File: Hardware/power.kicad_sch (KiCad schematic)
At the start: 12 parts, among them J1 Barrel_Jack_MountingPin, J2 31-M-12, Q1 AONR21321, U1 HUSB238, U2 AMS1117-3.3

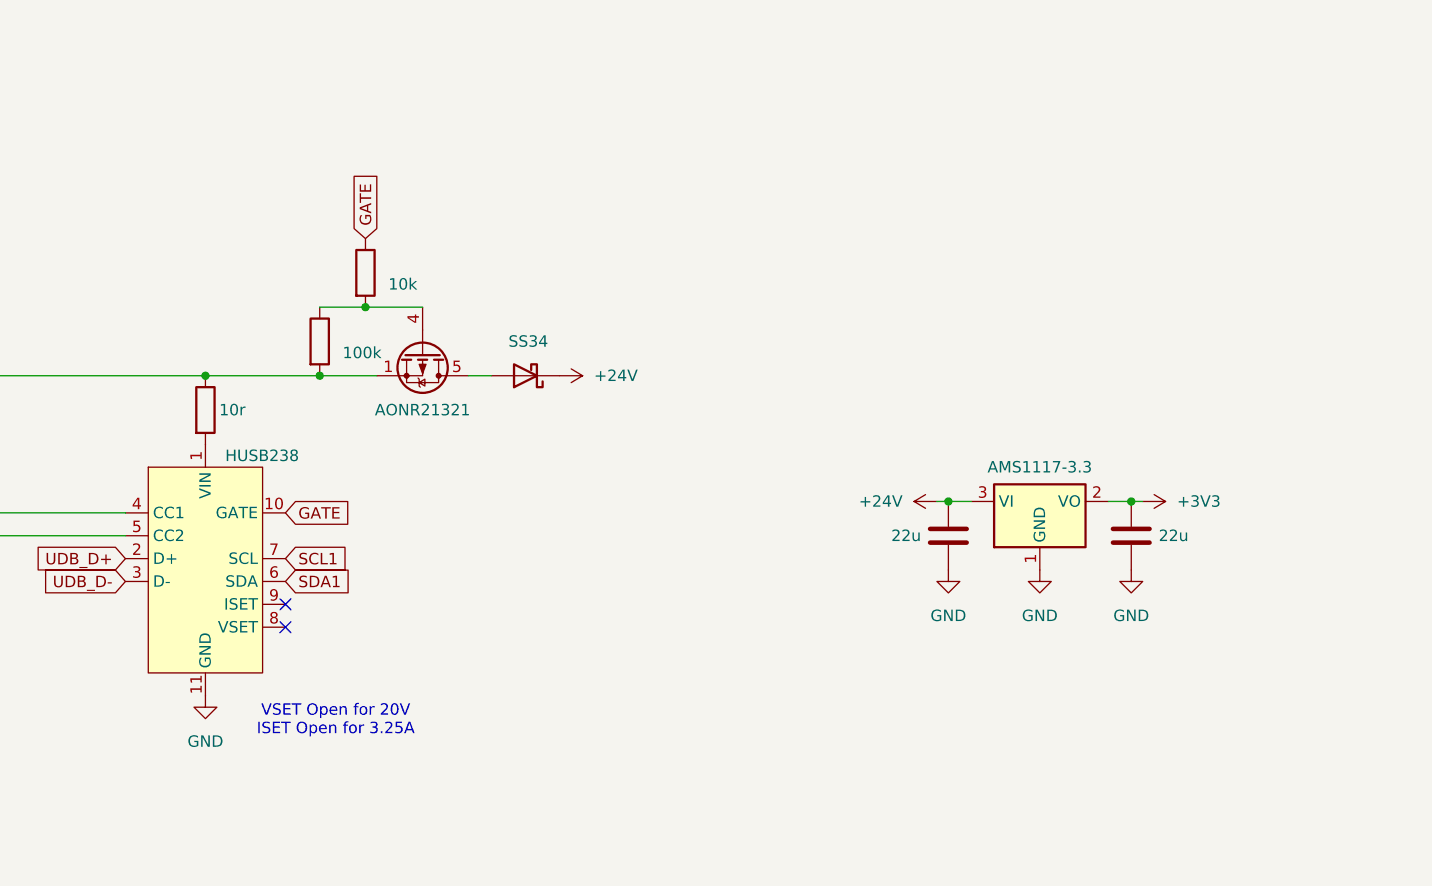
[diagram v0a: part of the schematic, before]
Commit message: Add readme, bad power routing, final heater idea. Likely needs new layout.
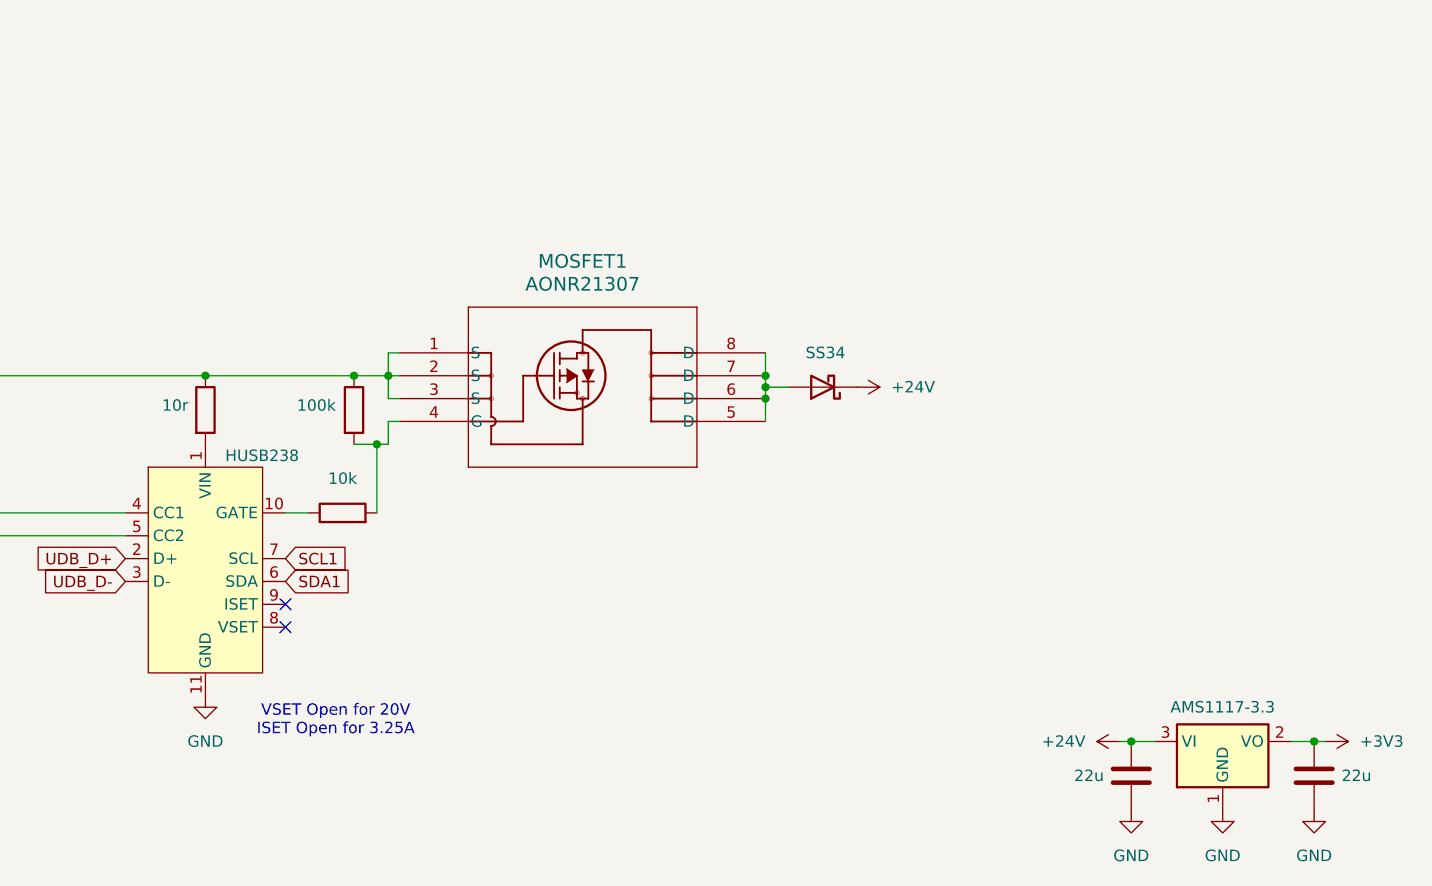
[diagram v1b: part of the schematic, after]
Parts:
- removed Q1: AONR21321, Package_DFN_QFN:AO_DFN-8-1EP_5.55x5.2mm_P1.27mm_EP4.12x4.6mm, symbol Transistor_FET:AON6411
- added MOSFET1: AONR21307, DFN8_3x3_EP_AOS, symbol 2024-03-28_00-32-34:AONR21307
- J1: footprint (none) -> footprints:DC Barrel
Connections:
- net at J2.A4 (VBUS), J2.A9 (VBUS), J2.B4 (VBUS)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: now also R2.1, MOSFET1.1 (S), MOSFET1.2 (S), MOSFET1.3 (S); no longer R2.2
- net at R1.2: now also R2.2, MOSFET1.4 (G); no longer R2.1
- net at D2.2 (A): now also MOSFET1.5 (D), MOSFET1.6 (D), MOSFET1.7 (D), MOSFET1.8 (D)
- net GATE: no longer names the net of R1.1, U1.10 (GATE)

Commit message: Closer to final placement of power components. Shooting for single sided assembly. Still some scuffed placements. Really packed. Missing likely needed ground planes.
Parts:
- D1, D2: footprint Diode_SMD:D_SMA -> Diode_SMD:D_SOD-123
- MOSFET1: footprint DFN8_3x3_EP_AOS -> footprints:DFN8_3x3_EP_AOS
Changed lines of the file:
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@@
+	)
+	(symbol
+		(lib_id "Device:D_Schottky")
+		(at 203.2 88.9 180)
+		(unit 1)
+		(exclude_from_sim no)
+		(in_bom yes)
+		(on_board yes)
+		(dnp no)
+		(fields_autoplaced yes)
+		(property "Reference" "D2"
+			(at 203.5175 82.55 0)
+			(effects
+				(font
+					(size 1.27 1.27)
+				)
+				(hide yes)
+			)
+		)
+		(property "Value" "SS34"
+			(at 203.5175 85.09 0)
+			(effects
+				(font
+					(size 1.27 1.27)
+				)
+			)
+		)
+		(property "Footprint" "Diode_SMD:D_SOD-123"
+			(at 203.2 88.9 0)
+			(effects
+				(font
+					(size 1.27 1.27)
+				)
+				(hide yes)
+			)
+		)
+		(property "Datasheet" "~"
+			(at 203.2 88.9 0)
+			(effects
+				(font
+					(size 1.27 1.27)
+				)
+				(hide yes)
+			)
+		)
+		(property "Description" "Schottky diode"
+			(at 203.2 88.9 0)
+			(effects
+				(font
+					(size 1.27 1.27)
+				)
+				(hide yes)
+			)
+		)
+		(pin "2"
+		)
+		(pin "1"
+		)
+		(instances
+			(project "Reflow Plate"
+				(path "/49cd4b29-c85a-4a2b-85b7-8d851eb45e3f/984a2abf-7e27-43b4-9e42-972d8cbed76d"
+					(reference "D2")
+					(unit 1)
+				)
+			)
+		)
 	)
 	(symbol
@@
 			)
 		)
-		(property "Footprint" "DFN8_3x3_EP_AOS"
+		(property "Footprint" "footprints:DFN8_3x3_EP_AOS"
 			(at 156.21 85.09 0)
 			(effects
@@
 	)
 	(symbol
-		(lib_id "Device:D_Schottky")
-		(at 203.2 88.9 180)
-		(unit 1)
-		(exclude_from_sim no)
-		(in_bom yes)
-		(on_board yes)
-		(dnp no)
-		(fields_autoplaced yes)
-		(property "Reference" "D2"
-			(at 203.5175 82.55 0)
-			(effects
-				(font
-					(size 1.27 1.27)
-				)
-				(hide yes)
-			)
-		)
-		(property "Value" "SS34"
-			(at 203.5175 85.09 0)
-			(effects
-				(font
-					(size 1.27 1.27)
-				)
-			)
-		)
-		(property "Footprint" "Diode_SMD:D_SMA"
-			(at 203.2 88.9 0)
-			(effects
-				(font
-					(size 1.27 1.27)
-				)
-				(hide yes)
-			)
-		)
-		(property "Datasheet" "~"
-			(at 203.2 88.9 0)
-			(effects
-				(font
-					(size 1.27 1.27)
-				)
-				(hide yes)
-			)
-		)
-		(property "Description" "Schottky diode"
-			(at 203.2 88.9 0)
-			(effects
-				(font
-					(size 1.27 1.27)
-				)
-				(hide yes)
-			)
-		)
-		(pin "2"
-		)
-		(pin "1"
-		)
-		(instances
-			(project "Reflow Plate"
-				(path "/49cd4b29-c85a-4a2b-85b7-8d851eb45e3f/984a2abf-7e27-43b4-9e42-972d8cbed76d"
-					(reference "D2")
-					(unit 1)
-				)
-			)
-		)
-	)
-	(symbol
 		(lib_id "Device:C")
 		(at 257.81 132.08 0)
@@
 			)
 		)
-		(property "Footprint" "Diode_SMD:D_SMA"
+		(property "Footprint" "Diode_SMD:D_SOD-123"
 			(at 90.17 52.07 0)
 			(effects

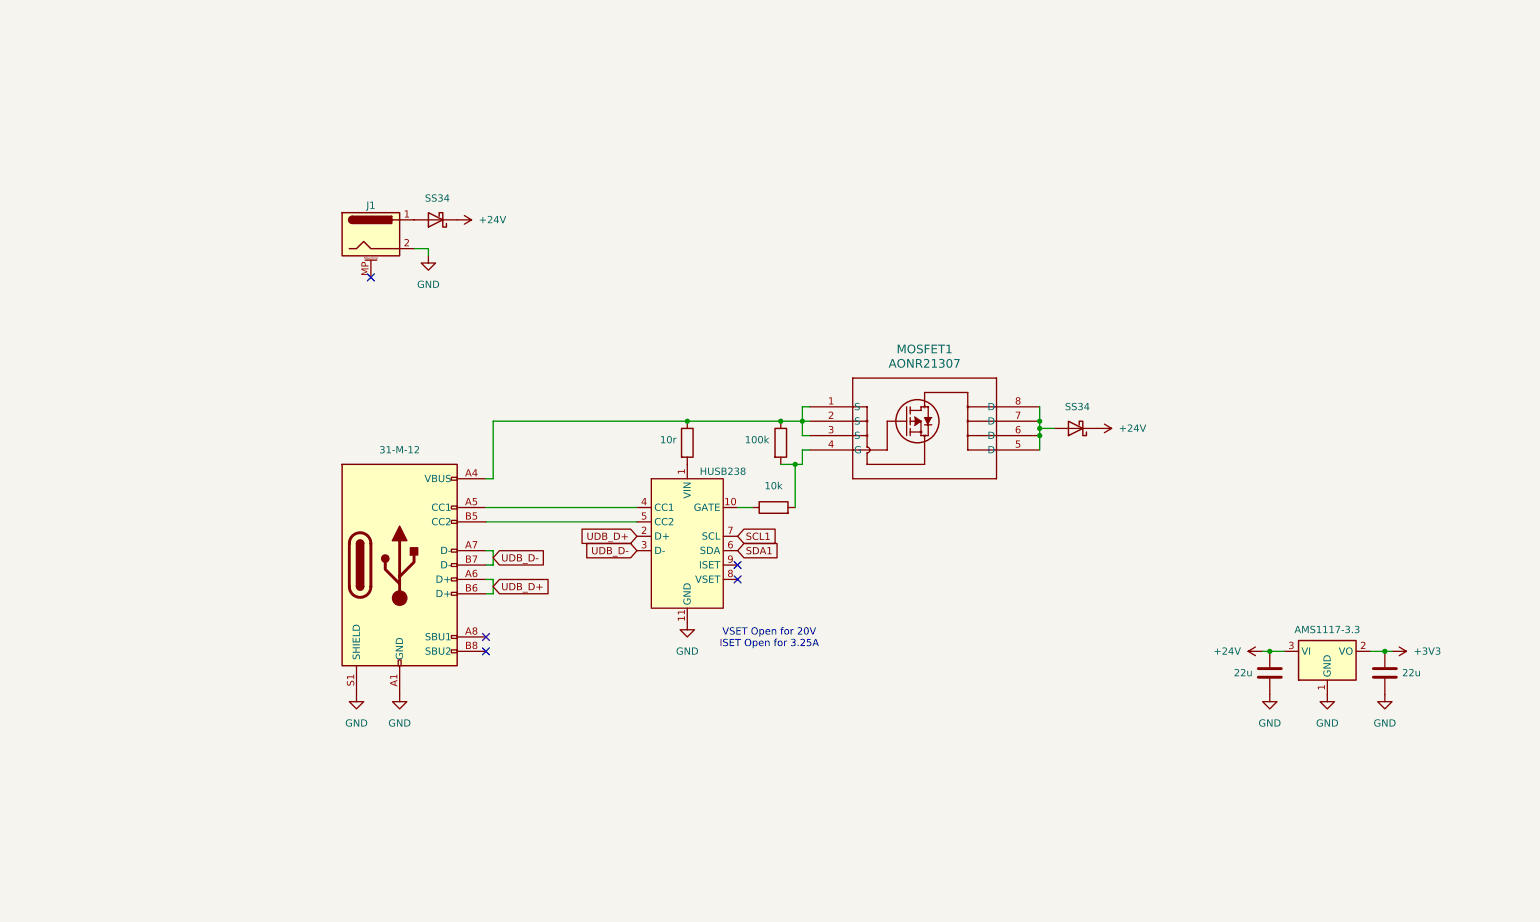
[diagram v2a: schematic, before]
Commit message: Ditch rev 1, moving on to rev 2.
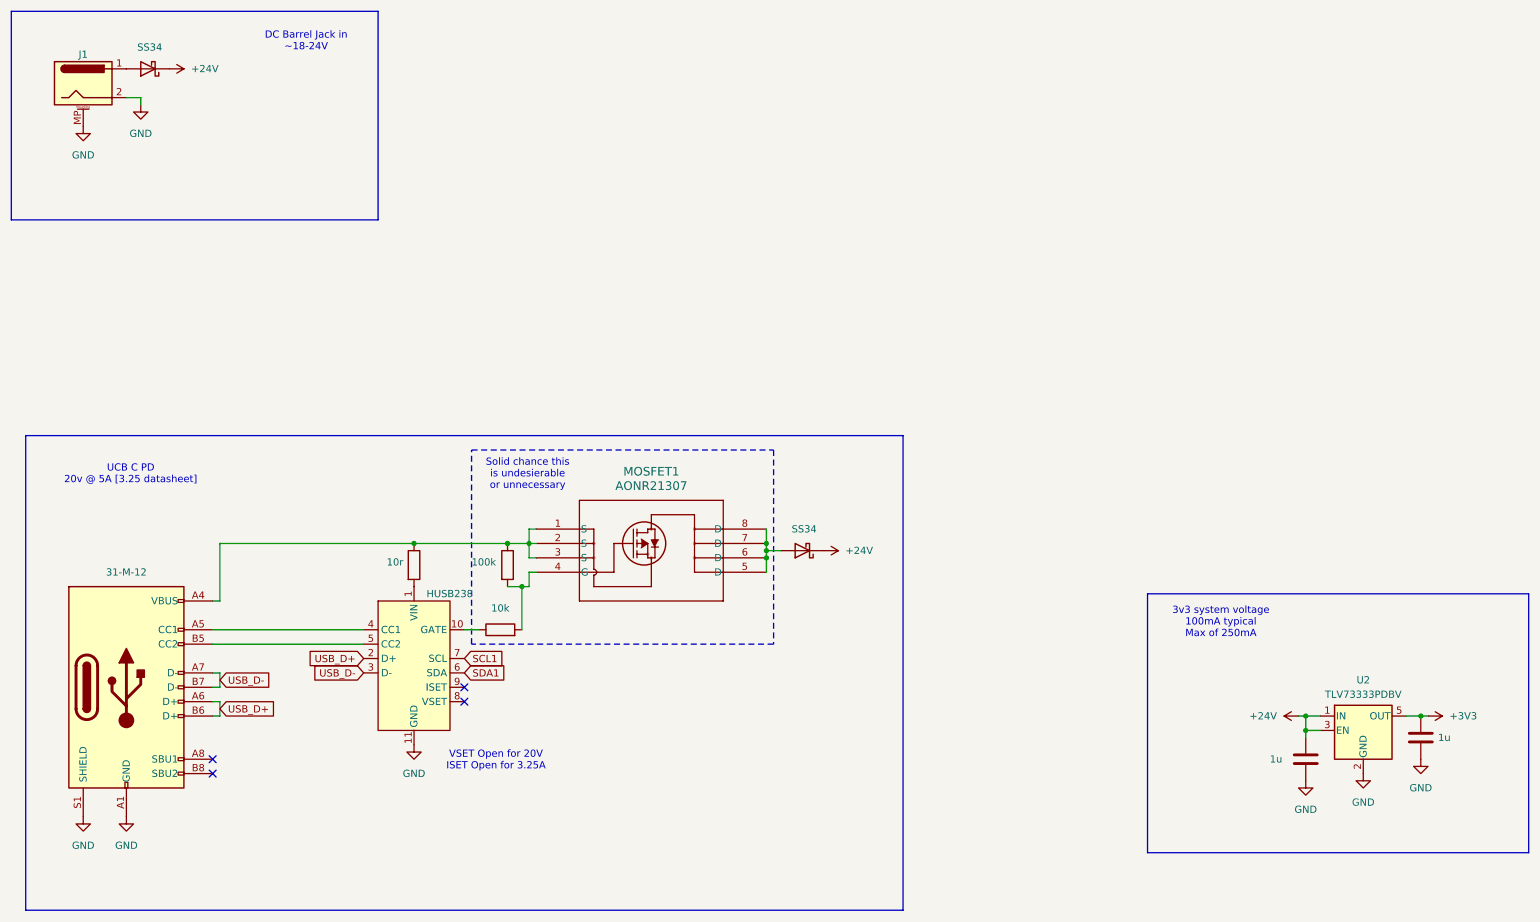
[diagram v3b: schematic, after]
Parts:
- removed U2: AMS1117-3.3, Package_TO_SOT_SMD:SOT-223-3_TabPin2, symbol Regulator_Linear:AMS1117-3.3
- added U2: TLV73333PDBV, Package_TO_SOT_SMD:SOT-23-5, symbol Regulator_Linear:TLV73333PDBV
- C1, C2: value 22u -> 1u; footprint Capacitor_SMD:C_0805_2012Metric -> Capacitor_SMD:C_0402_1005Metric
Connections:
- net +24V: now also U2.1 (IN), U2.3 (EN)
- net +3V3: now also U2.5 (OUT)
- net GND: now also J1.MP (MountPin), U2.2 (GND)
- net UDB_D+ renamed USB_D+
- net UDB_D- renamed USB_D-
- no-connect marks 5 -> 4
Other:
- note added: "3v3 system voltage 100mA typical Max of 250mA"
- note added: "DC Barrel Jack in ~18-24V"
- note added: "Solid chance this is undesierable or unnecessary"
- note added: "UCB C PD 20v @ 5A [3.25 datasheet]"
- moved on the sheet: J1, MOSFET1

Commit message: Rev 'b'. Having this produced. Added some voltage monitors. cleaned up traces. Moved i2c lines to i2c2. forgot to add pull-ups. the ones in the display should work though.
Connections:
- net +24V renamed VBUS
